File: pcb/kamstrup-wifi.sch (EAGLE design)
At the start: 5 parts

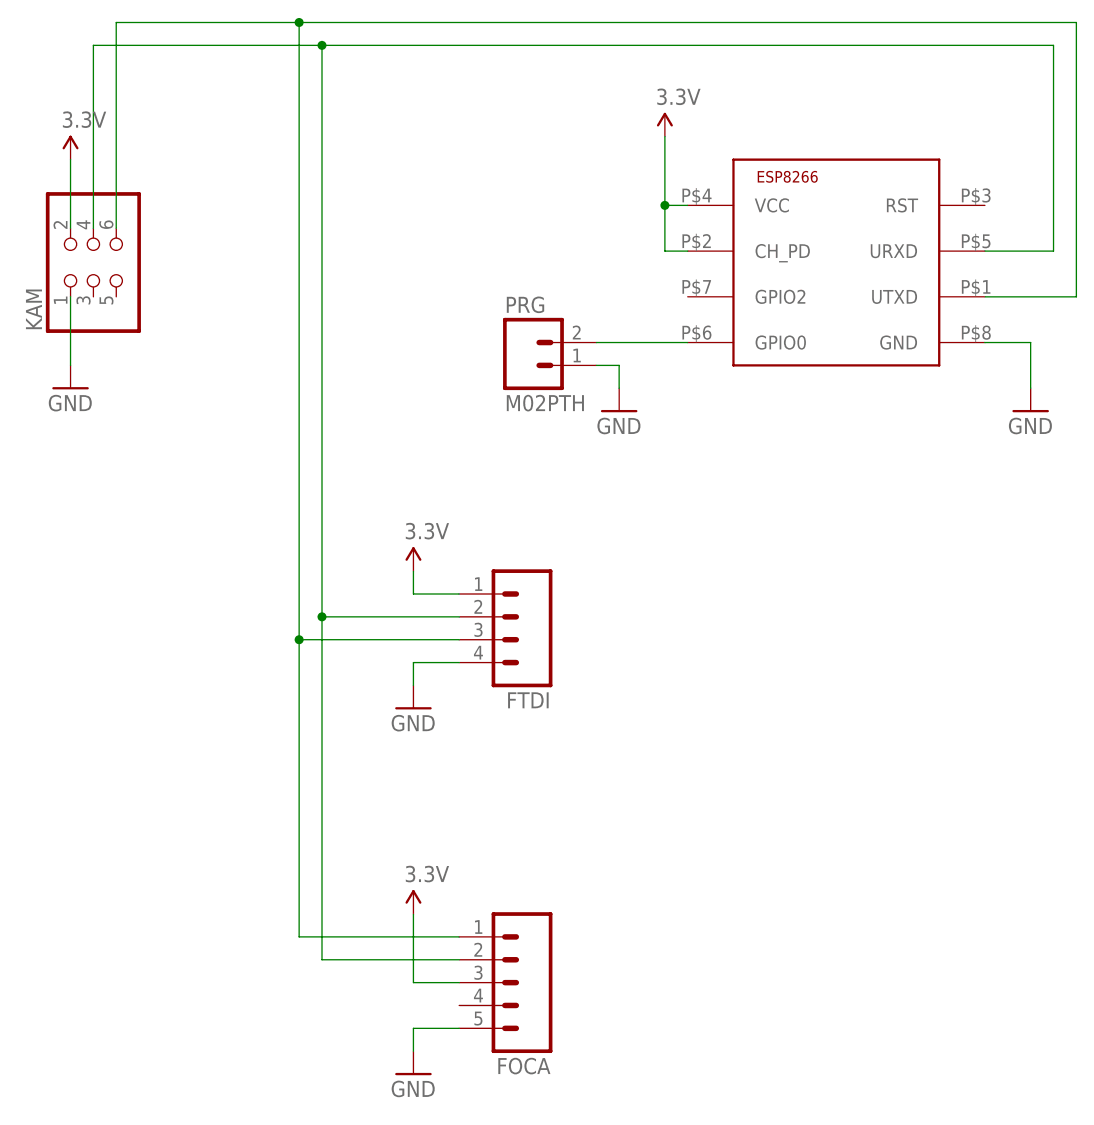
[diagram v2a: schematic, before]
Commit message: pcb: names on ftdi pins
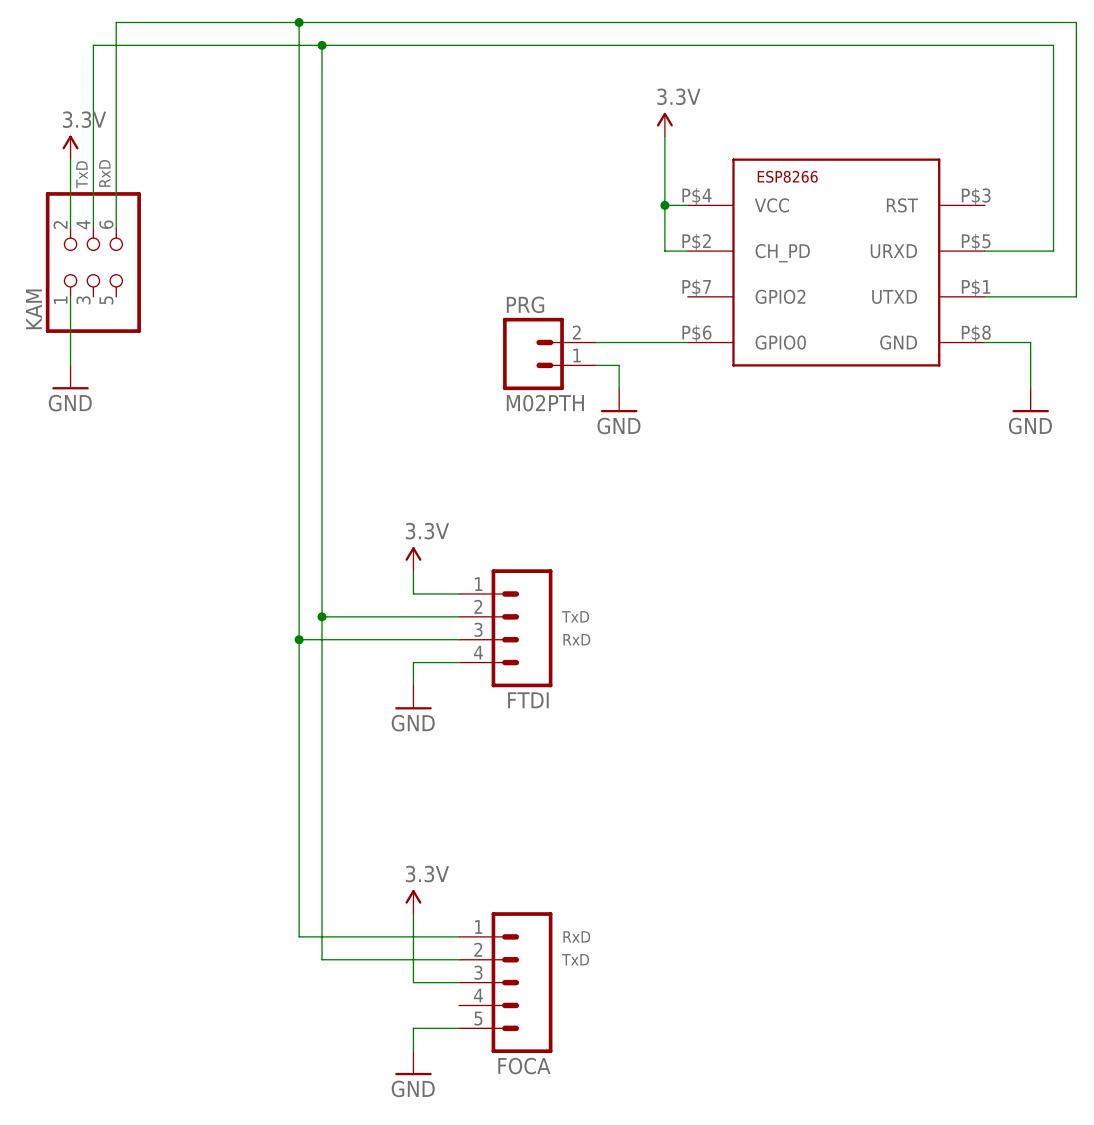
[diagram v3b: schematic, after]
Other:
- note added: "RxD"
- note added: "TxD"
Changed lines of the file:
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@@
 <setting verticaltext="up"/>
 </settings>
-<grid distance="0.1" unitdist="inch" unit="inch" style="lines" multiple="1" display="no" altdistance="0.01" altunitdist="inch" altunit="inch"/>
+<grid distance="0.05" unitdist="inch" unit="inch" style="lines" multiple="1" display="no" altdistance="0.005" altunitdist="inch" altunit="inch"/>
 <layers>
 <layer number="1" name="Top" color="4" fill="1" visible="no" active="no"/>
@@
 <sheet>
 <plain>
+<text x="17.145" y="73.025" size="1.27" layer="95" rot="R90">RxD</text>
+<text x="14.605" y="73.025" size="1.27" layer="95" rot="R90">TxD</text>
+<text x="67.31" y="24.765" size="1.27" layer="95" rot="R180" align="top-right">TxD</text>
+<text x="67.31" y="22.225" size="1.27" layer="95" rot="R180" align="top-right">RxD</text>
+<text x="67.31" y="-10.795" size="1.27" layer="95" rot="R180" align="top-right">RxD</text>
+<text x="67.31" y="-13.335" size="1.27" layer="95" rot="R180" align="top-right">TxD</text>
 </plain>
 <instances>

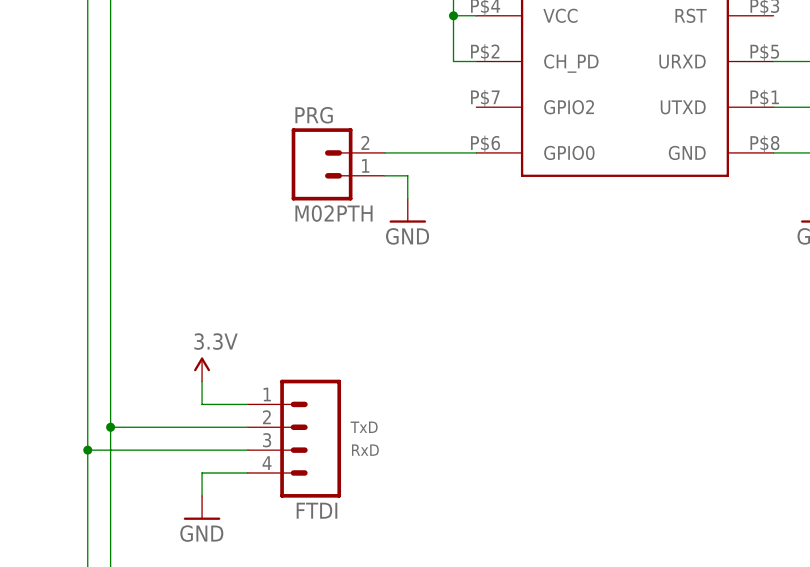
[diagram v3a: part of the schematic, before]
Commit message: pull down resistor on gpio0
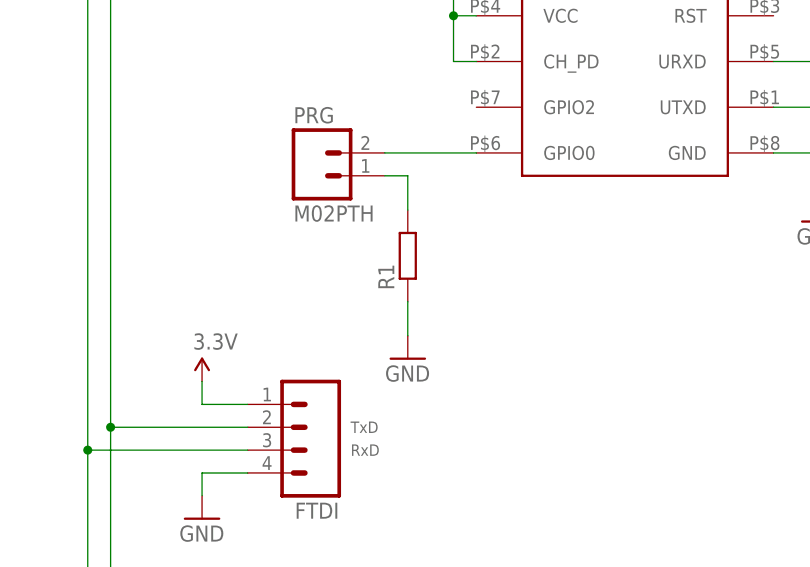
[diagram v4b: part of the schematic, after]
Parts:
- added R1: (no value), resistor:R-EU_M0805
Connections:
- new net N$4: PRG.1, R1.2
- net GND: now also R1.1; no longer PRG.1
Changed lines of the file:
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@@
 <layer number="97" name="Info" color="7" fill="1" visible="yes" active="yes"/>
 <layer number="98" name="Guide" color="6" fill="1" visible="yes" active="yes"/>
+<layer number="99" name="SpiceOrder" color="5" fill="1" visible="yes" active="yes"/>
 <layer number="100" name="Muster" color="7" fill="1" visible="no" active="no"/>
 <layer number="101" name="Patch_Top" color="12" fill="4" visible="yes" active="yes"/>
@@
 <part name="PRG" library="SparkFun-Connectors" deviceset="M02" device="PTH"/>
 <part name="GND5" library="SparkFun-Aesthetics" deviceset="GND" device=""/>
+<part name="R1" library="resistor" deviceset="R-EU_" device="M0805"/>
 </parts>
 <sheets>
@@
 <attribute name="NAME" x="60.96" y="59.182" size="1.778" layer="95"/>
 </instance>
-<instance part="GND5" gate="1" x="73.66" y="48.26"/>
+<instance part="GND5" gate="1" x="73.66" y="33.02"/>
+<instance part="R1" gate="G$1" x="73.66" y="44.45" rot="R90"/>
 </instances>
 <busses>
@@
 </segment>
 <segment>
-<pinref part="PRG" gate="G$1" pin="1"/>
 <pinref part="GND5" gate="1" pin="GND"/>
-<wire x1="71.12" y1="53.34" x2="73.66" y2="53.34" width="0.1524" layer="91"/>
-<wire x1="73.66" y1="53.34" x2="73.66" y2="50.8" width="0.1524" layer="91"/>
+<pinref part="R1" gate="G$1" pin="1"/>
+<wire x1="73.66" y1="35.56" x2="73.66" y2="39.37" width="0.1524" layer="91"/>
 </segment>
 </net>
@@
 </segment>
 </net>
+<net name="N$4" class="0">
+<segment>
+<pinref part="PRG" gate="G$1" pin="1"/>
+<wire x1="71.12" y1="53.34" x2="73.66" y2="53.34" width="0.1524" layer="91"/>
+<pinref part="R1" gate="G$1" pin="2"/>
+<wire x1="73.66" y1="53.34" x2="73.66" y2="49.53" width="0.1524" layer="91"/>
+</segment>
+</net>

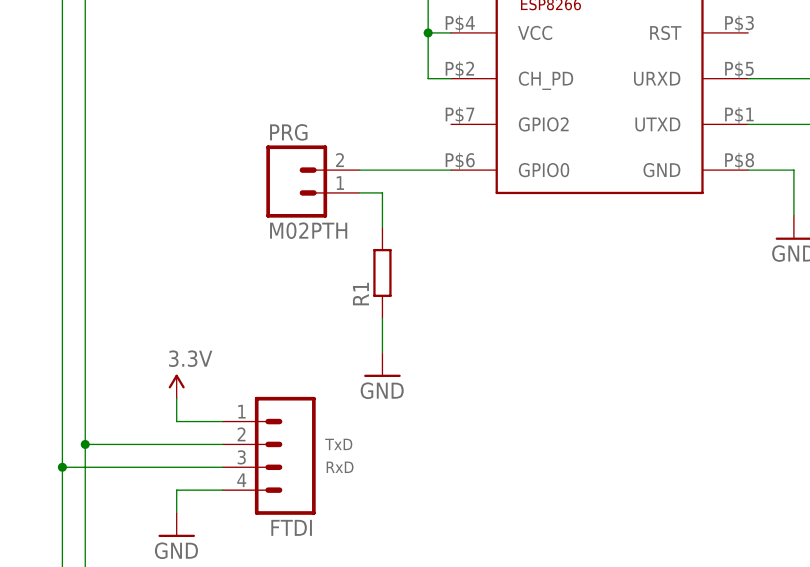
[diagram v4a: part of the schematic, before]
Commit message: pull down resisistor value = 10k
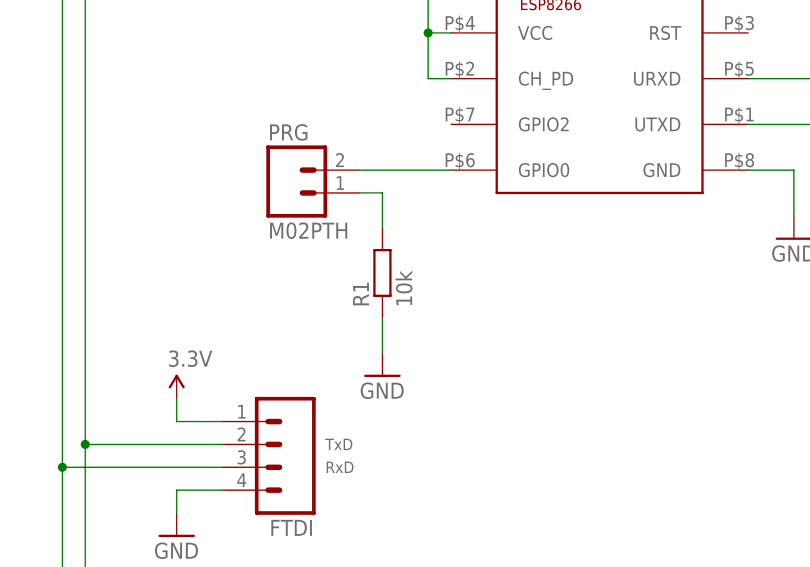
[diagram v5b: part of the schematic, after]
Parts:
- R1: value (none) -> 10k
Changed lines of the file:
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@@
 <part name="PRG" library="SparkFun-Connectors" deviceset="M02" device="PTH"/>
 <part name="GND5" library="SparkFun-Aesthetics" deviceset="GND" device=""/>
-<part name="R1" library="resistor" deviceset="R-EU_" device="M0805"/>
+<part name="R1" library="resistor" deviceset="R-EU_" device="M0805" value="10k"/>
 </parts>
 <sheets>
